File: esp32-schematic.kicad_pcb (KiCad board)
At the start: 2 copper layers, 1 part, among them U1 ESP32-S3-DEVKITC-1U-N8R2

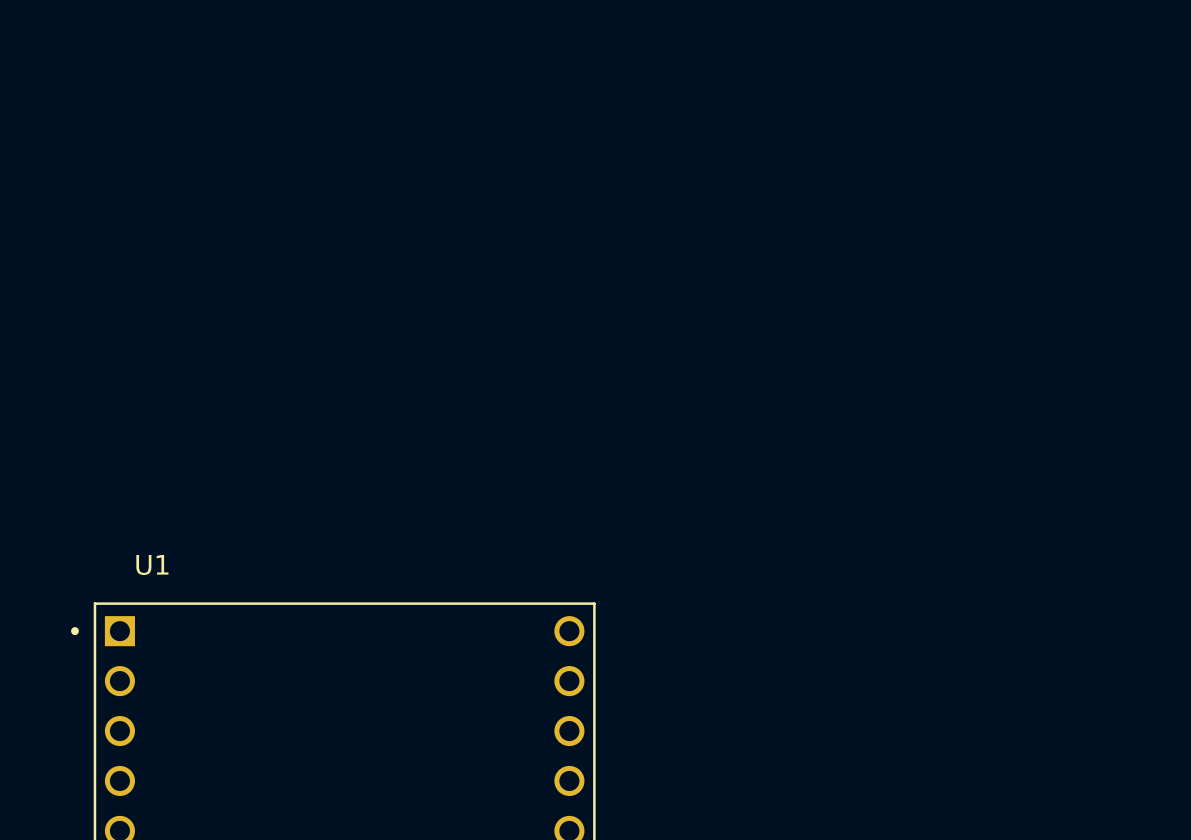
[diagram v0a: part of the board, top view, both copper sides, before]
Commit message: GPS added and CAN in progress
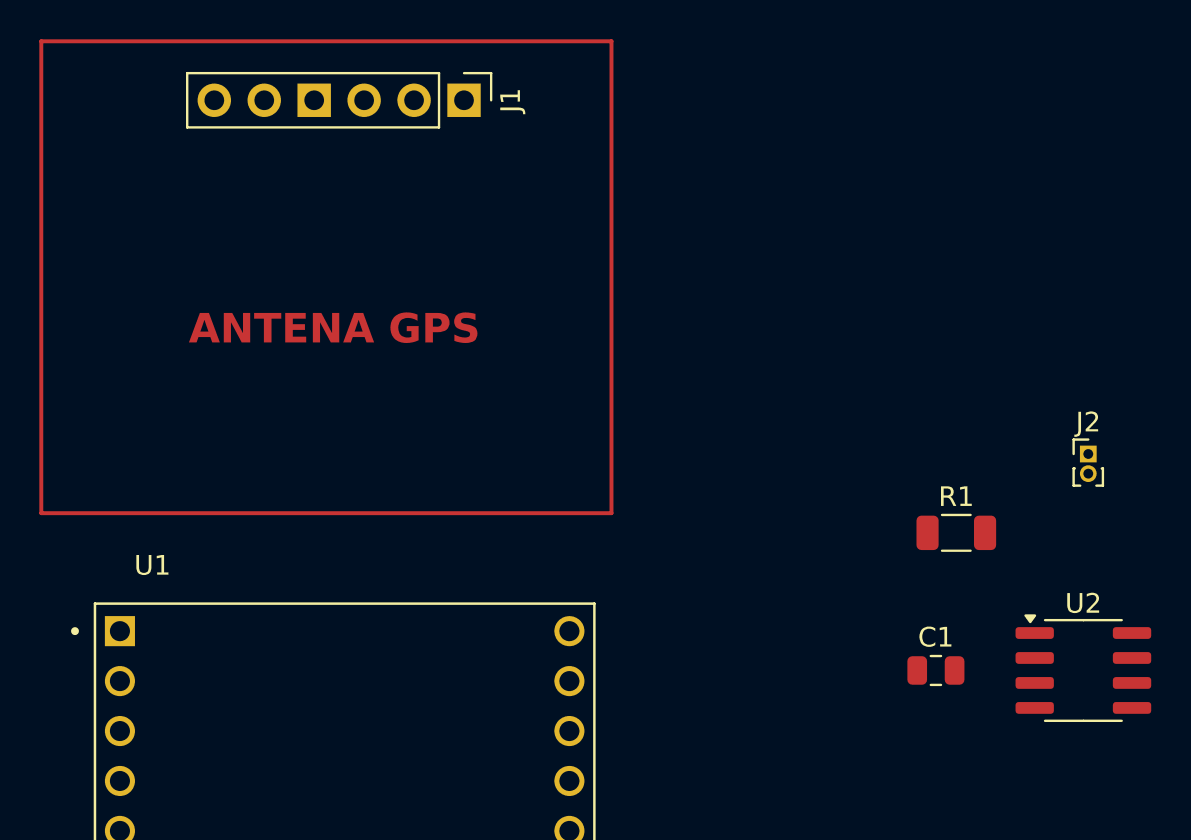
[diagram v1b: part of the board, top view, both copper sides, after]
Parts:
- added C1: 100pF, Capacitor_SMD:C_0805_2012Metric, F.Cu at (111.0, 46.5)
- added J1: GPS, Conn_01x06:PinHeader_1x06_P2.54mm_Vertical, F.Cu at (87.0, 17.5)
- added J2: Jumper, Connector_PinHeader_1.00mm:PinHeader_1x02_P1.00mm_Vertical, F.Cu at (118.8, 35.5)
- added R1: 120R, Resistor_SMD:R_1206_3216Metric, F.Cu at (112.0, 39.5)
- added U2: TJA1051T, Package_SO:SOIC-8_3.9x4.9mm_P1.27mm, F.Cu at (118.5, 46.5)
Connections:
- net Net-(U1-3V3-PadJ1_1) renamed 3.3V
- net Net-(U1-GND-PadJ1_22) renamed GND
- U1 pad J1_21: unconnected-(U1-5V0-PadJ1_21) -> 5V
- U1 pad J1_5: unconnected-(U1-GPIO5-PadJ1_5) -> PPS
- U1 pad J3_2: unconnected-(U1-U0TXD/GPIO43-PadJ3_2) -> TX
- U1 pad J3_3: unconnected-(U1-U0RXD/GPIO44-PadJ3_3) -> RX
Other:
- board text added: "ANTENA GPS"

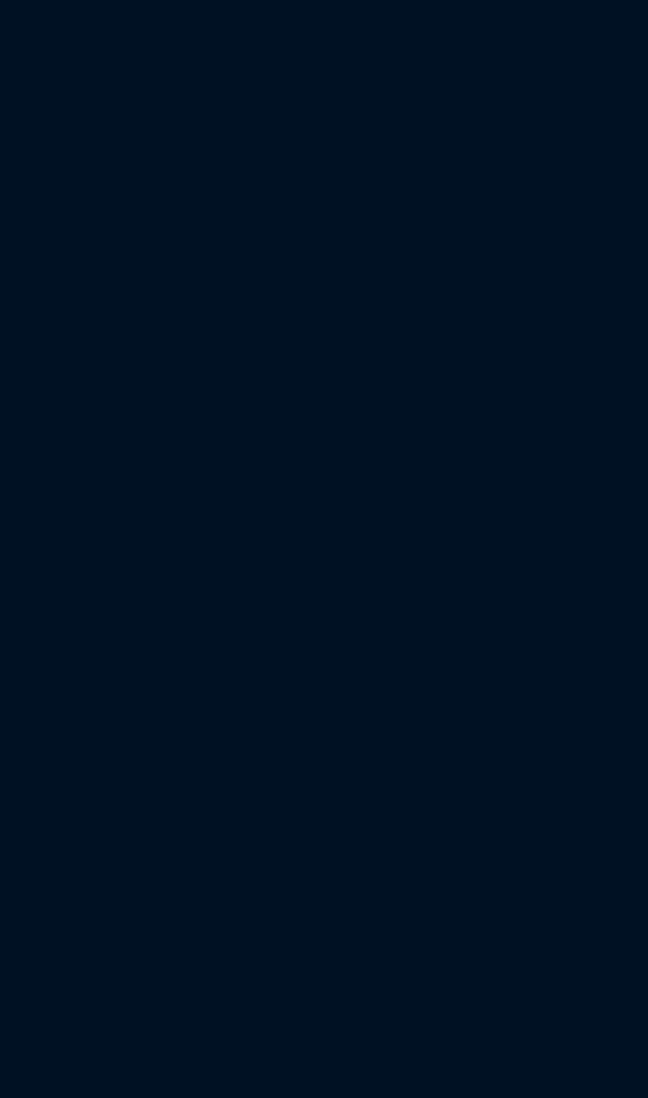
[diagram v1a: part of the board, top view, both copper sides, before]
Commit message: CAN schematic and IMU schematic ready
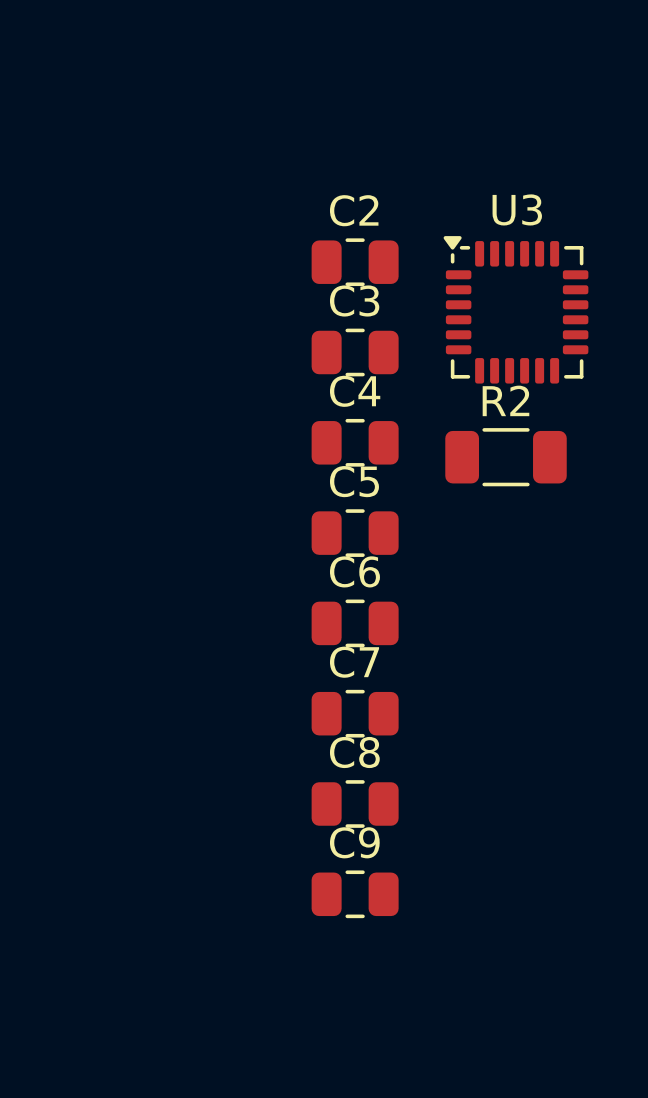
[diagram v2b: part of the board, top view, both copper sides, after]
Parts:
- added C2: 0.1uF, Capacitor_SMD:C_0805_2012Metric, F.Cu at (138.9, 56.4)
- added C3: 47uF, Capacitor_SMD:C_0805_2012Metric, F.Cu at (138.9, 59.4)
- added C4: 0.1uF, Capacitor_SMD:C_0805_2012Metric, F.Cu at (138.9, 62.5)
- added C5: 100nF, Capacitor_SMD:C_0805_2012Metric, F.Cu at (138.9, 65.5)
- added C6: 100nF, Capacitor_SMD:C_0805_2012Metric, F.Cu at (138.9, 68.5)
- added C7: 100nF, Capacitor_SMD:C_0805_2012Metric, F.Cu at (138.9, 71.5)
- added C8: 1uF, Capacitor_SMD:C_0805_2012Metric, F.Cu at (138.9, 74.5)
- added C9: 100nF, Capacitor_SMD:C_0805_2012Metric, F.Cu at (138.9, 77.5)
- added R2: 120R, Resistor_SMD:R_1206_3216Metric, F.Cu at (144.0, 62.9)
- added U3: MPU-6000, Sensor_Motion:InvenSense_QFN-24_4x4mm_P0.5mm, F.Cu at (144.3, 58.1)
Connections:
- J1 pad 1: 3.3V -> unconnected-(J1-Pin_1-Pad1)
- J1 pad 2: PPS -> unconnected-(J1-Pin_2-Pad2)
- J1 pad 6: 5V -> GPIO17
- U1 pad J1_10: unconnected-(U1-GPIO17-PadJ1_10) -> GPIO17
- U2 pad 1: unconnected-(U2-TXD-Pad1) -> TX
- U2 pad 2: unconnected-(U2-GND-Pad2) -> GND
- U2 pad 3: unconnected-(U2-VCC-Pad3) -> 3.3V
- U2 pad 4: unconnected-(U2-RXD-Pad4) -> RX
- U2 pad 8: unconnected-(U2-S-Pad8) -> S

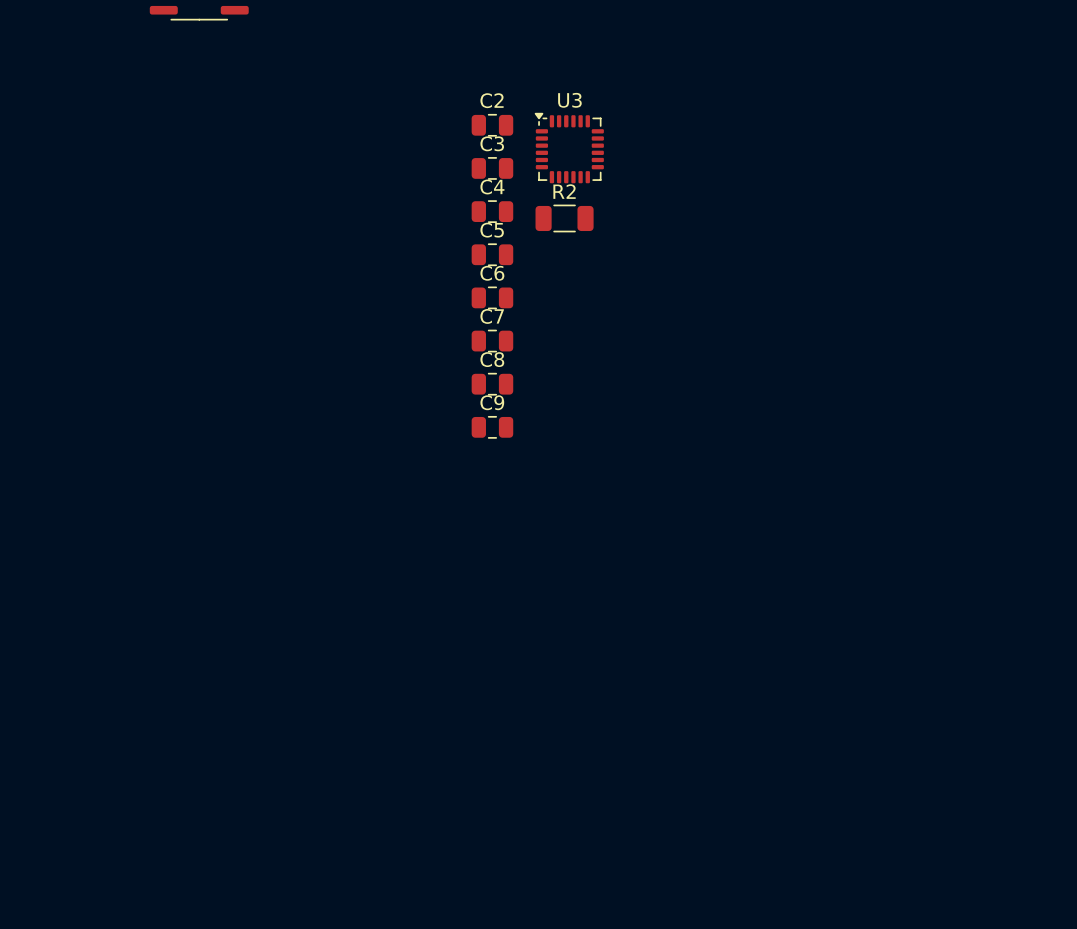
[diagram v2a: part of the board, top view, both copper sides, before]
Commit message: Micro SD added, IMU is now the MPU-9250, connections were moved in the ESP32 pins and the right footprints were added
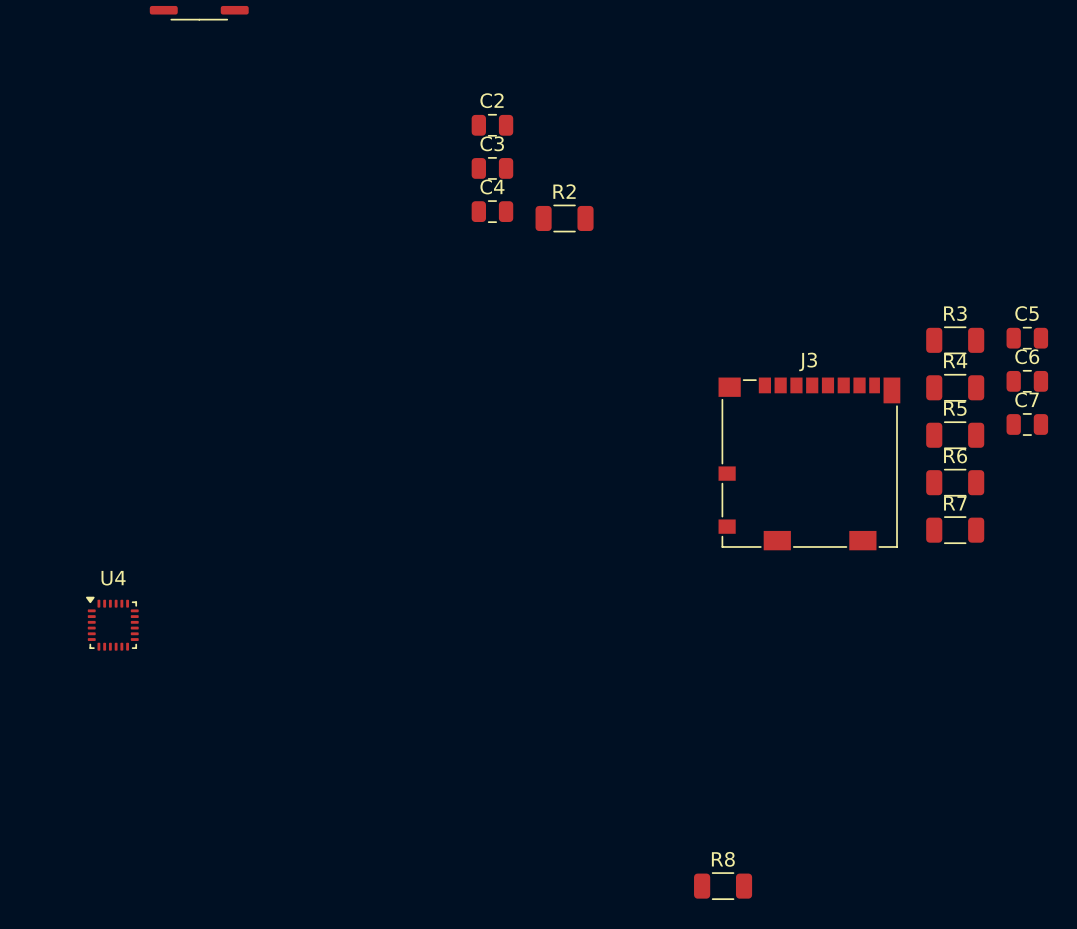
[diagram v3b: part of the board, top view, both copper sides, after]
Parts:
- removed C8: 1uF, Capacitor_SMD:C_0805_2012Metric
- removed C9: 100nF, Capacitor_SMD:C_0805_2012Metric
- removed U3: MPU-6000, Sensor_Motion:InvenSense_QFN-24_4x4mm_P0.5mm
- added J3: Micro_SD_Card, Connector_Card:microSD_HC_Molex_104031-0811, F.Cu at (161.1, 80.0)
- added R3: 10K, Resistor_SMD:R_1206_3216Metric, F.Cu at (171.2, 71.4)
- added R4: 10K, Resistor_SMD:R_1206_3216Metric, F.Cu at (171.2, 74.7)
- added R5: 10K, Resistor_SMD:R_1206_3216Metric, F.Cu at (171.2, 78.0)
- added R6: 10K, Resistor_SMD:R_1206_3216Metric, F.Cu at (171.2, 81.4)
- added R7: 10K, Resistor_SMD:R_1206_3216Metric, F.Cu at (171.2, 84.7)
- added R8: 10K, Resistor_SMD:R_1206_3216Metric, F.Cu at (155.0, 109.5)
- added U4: MPU-9250, Sensor_Motion:InvenSense_QFN-24_3x3mm_P0.4mm, F.Cu at (112.5, 91.3)
- C5, C7: value 100nF -> 0.1uF
- C6: value 100nF -> 0.01uF
- J1: value GPS -> GN-2630G
- moved C5 37.8 mm to (176.3, 71.3)
- moved C6 37.8 mm to (176.3, 74.3)
- moved C7 37.8 mm to (176.3, 77.3)
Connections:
- C5 pad 1: GND -> 3.3V
- C5 pad 2: 3.3V -> GND
- C6 pad 1: Net-(U3-REGOUT) -> 3.3V
- C7 pad 1: 3.3V -> Net-(U4-REGOUT)
- J1 pad 1: unconnected-(J1-Pin_1-Pad1) -> EN
- J1 pad 6: GPIO17 -> 5V
- U1 pad J1_10: GPIO17 -> unconnected-(U1-GPIO17-PadJ1_10)
- U1 pad J1_12: unconnected-(U1-GPIO8-PadJ1_12) -> SDA
- U1 pad J1_15: unconnected-(U1-GPIO9-PadJ1_15) -> SCL
- U1 pad J1_16: unconnected-(U1-GPIO10-PadJ1_16) -> CS
- U1 pad J1_17: unconnected-(U1-GPIO11-PadJ1_17) -> MOSI
- U1 pad J1_18: unconnected-(U1-GPIO12-PadJ1_18) -> CLK
- U1 pad J1_19: unconnected-(U1-GPIO13-PadJ1_19) -> MISO
- U1 pad J1_4: unconnected-(U1-GPIO4-PadJ1_4) -> EN
- U1 pad J1_5: PPS -> unconnected-(U1-GPIO5-PadJ1_5)
- U2 pad 3: 3.3V -> 5V

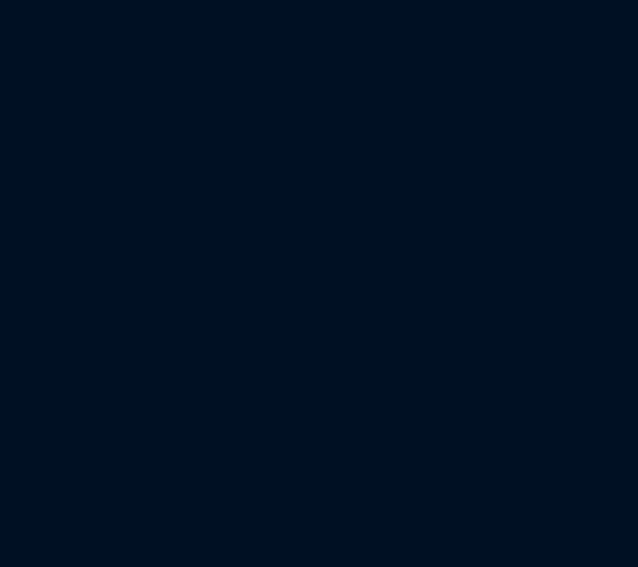
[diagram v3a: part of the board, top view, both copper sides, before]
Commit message: SD slot added, ENV added, issues fixed
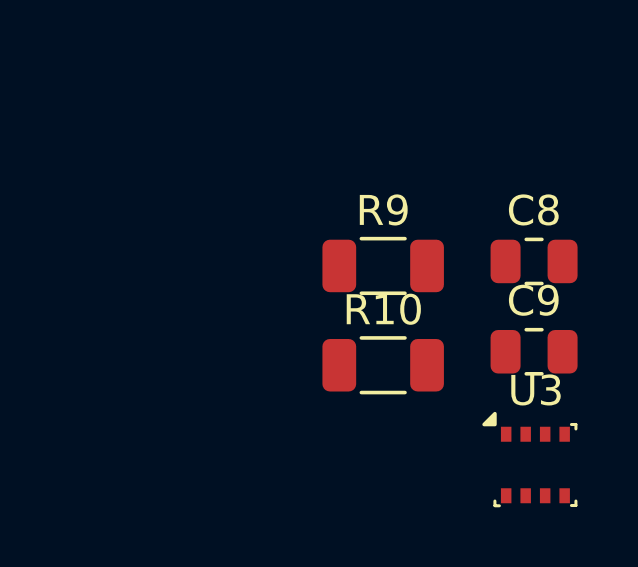
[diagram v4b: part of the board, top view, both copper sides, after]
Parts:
- added C8: 0.1uF, Capacitor_SMD:C_0805_2012Metric, F.Cu at (181.5, 109.2)
- added C9: 0.1uF, Capacitor_SMD:C_0805_2012Metric, F.Cu at (181.5, 112.2)
- added R10: 4.7K, Resistor_SMD:R_1206_3216Metric, F.Cu at (176.4, 112.7)
- added R9: 4.7K, Resistor_SMD:R_1206_3216Metric, F.Cu at (176.4, 109.3)
- added U3: BME280, Package_LGA:Bosch_LGA-8_2.5x2.5mm_P0.65mm_ClockwisePinNumbering, F.Cu at (181.5, 116.0)
